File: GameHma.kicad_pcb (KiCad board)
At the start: 2 copper layers, 98 x 82 mm, 19 parts, among them J1 Screw_Terminal_01x02, J2 Motor_Terminal_01x04, J3 Motor_Terminal_01x04, J4 Motor_Terminal_01x04, J5 Motor_Terminal_01x04, U1 ESP32-DEVKIT-V1, U2 A4988_STEPPER_MOTOR_DRIVER_CA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, U3 A4988_STEPPER_MOTOR_DRIVER_CA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, U4 A4988_STEPPER_MOTOR_DRIVER_CA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, U5 A4988_STEPPER_MOTOR_DRIVER_CA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, U6 SRT_MP1584EN

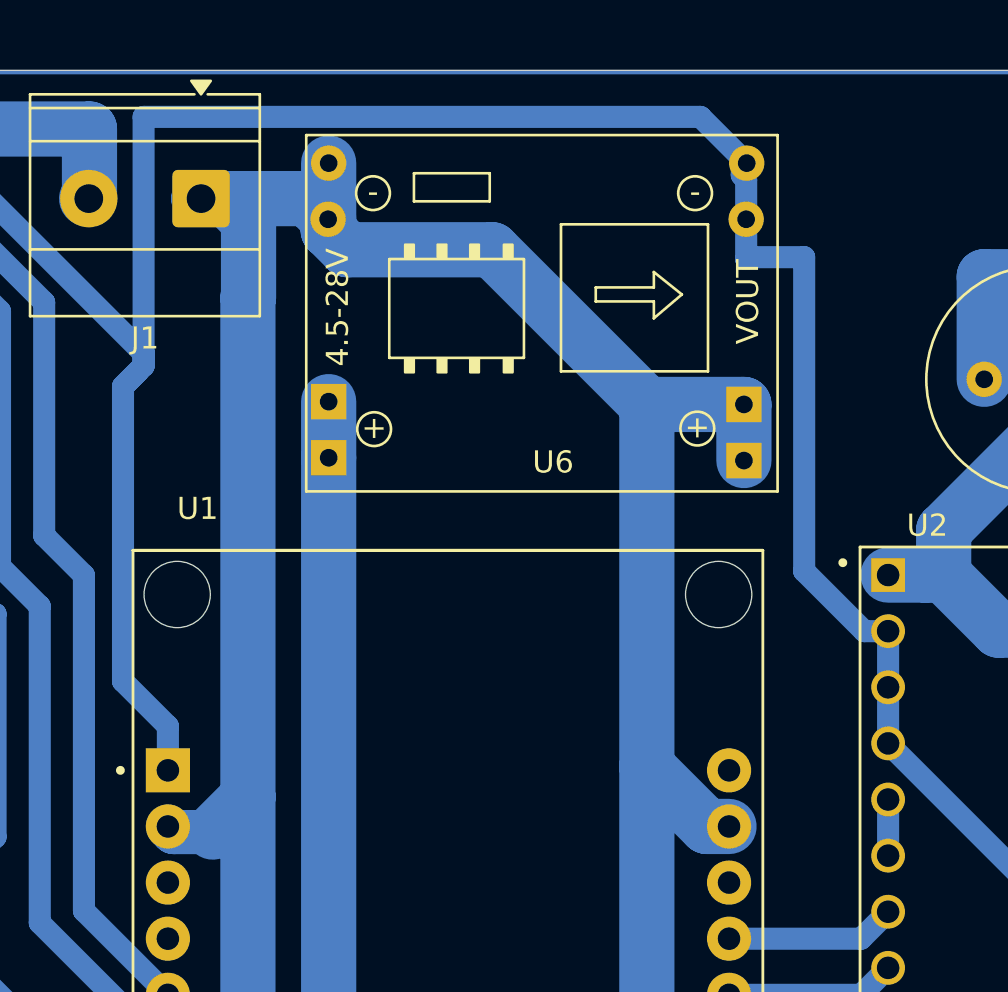
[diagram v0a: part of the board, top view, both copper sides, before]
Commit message: fix pin MP1584 footprint
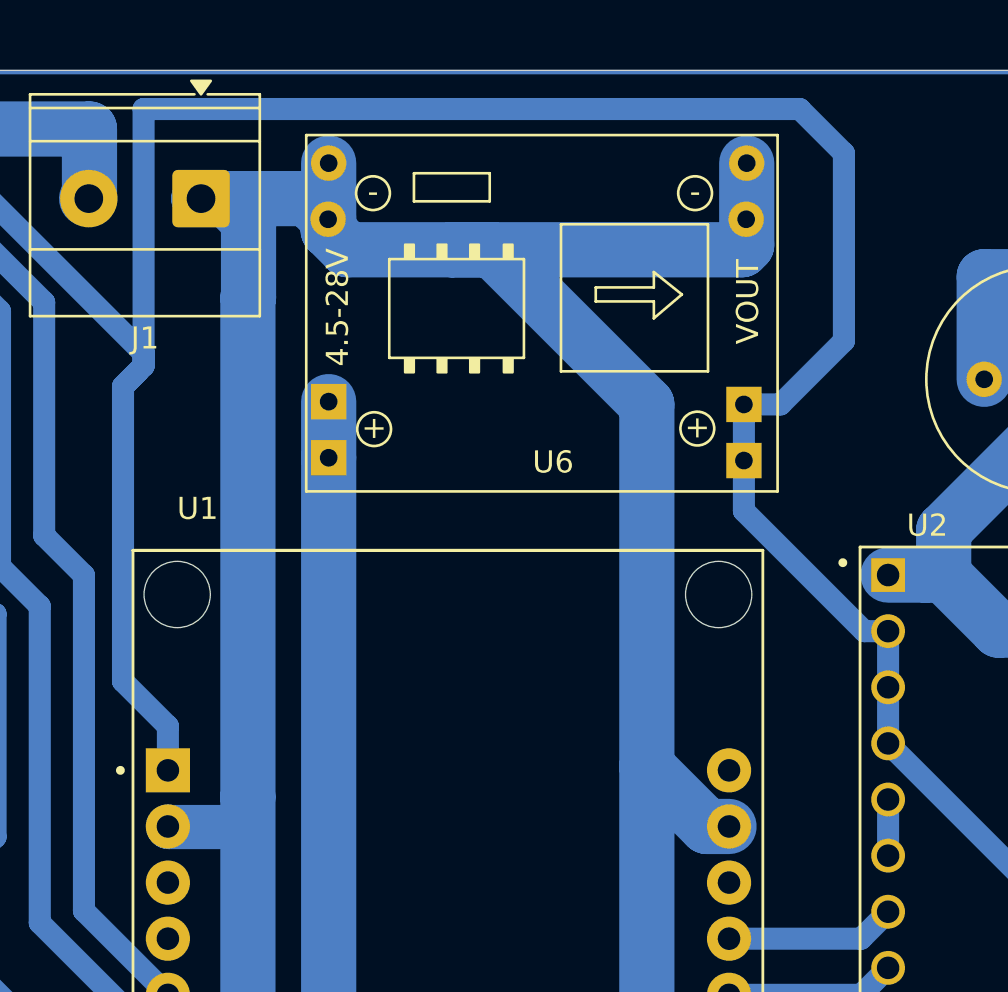
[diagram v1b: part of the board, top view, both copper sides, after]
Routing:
- net GND: track 467.1 -> 477.7 mm
- net +V_{DD}: track 252.3 -> 258.4 mm

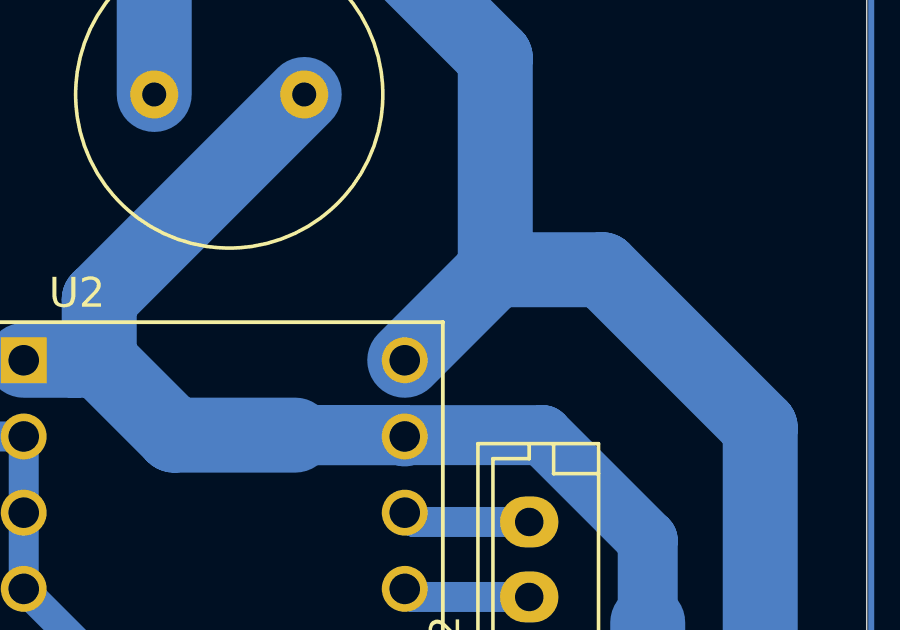
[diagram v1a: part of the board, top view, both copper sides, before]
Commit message: edit wire in U2 pin Vbatt at PCB editor
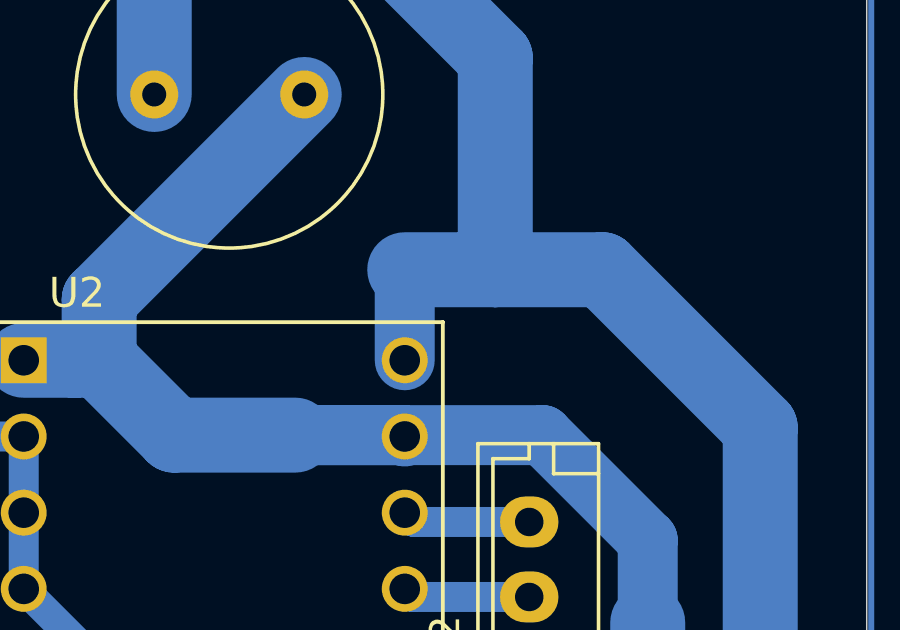
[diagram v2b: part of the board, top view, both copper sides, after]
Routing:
- net +V_{batt}: track 391.5 -> 393.2 mm
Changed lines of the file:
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@@
-	)
-	(segment
-		(start 182.2179 78.8271)
-		(end 179.2 81.845)
-		(width 2.5)
-		(layer "B.Cu")
-		(net 2)
 	)
 	(segment
@@
 	)
 	(segment
+		(start 182.2179 78.8271)
+		(end 179.2 78.8271)
+		(width 2.5)
+		(layer "B.Cu")
+		(net 2)
+	)
+	(segment
 		(start 110.95 122.655)
 		(end 100.5 122.655)
@@
 		(layer "B.Cu")
 		(net 2)
+	)
+	(segment
+		(start 179.2 81.845)
+		(end 179.2 78.8271)
+		(width 2)
+		(layer "B.Cu")
+		(net 2)

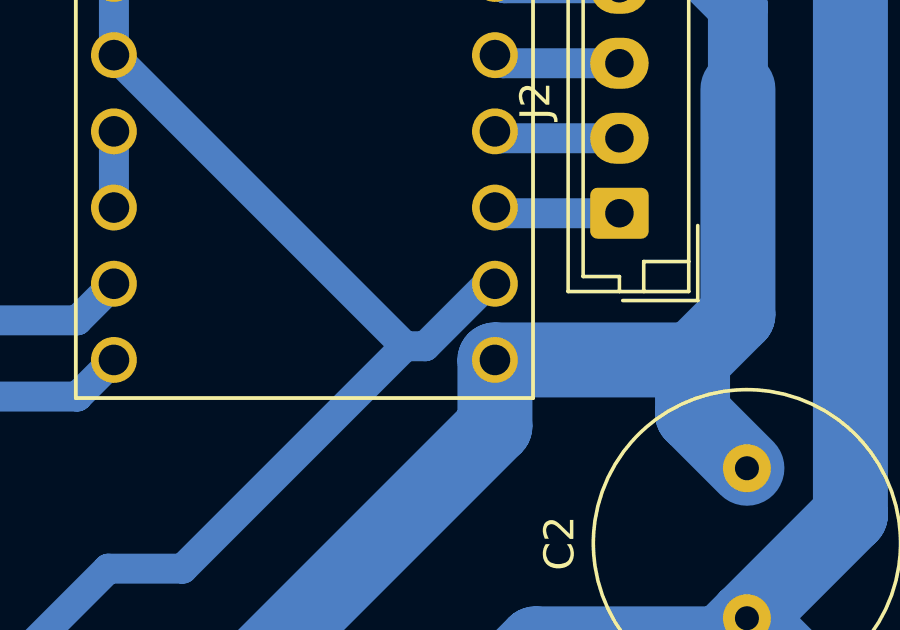
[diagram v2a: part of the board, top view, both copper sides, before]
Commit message: edit wire in U2 pin VDD at PCB editor
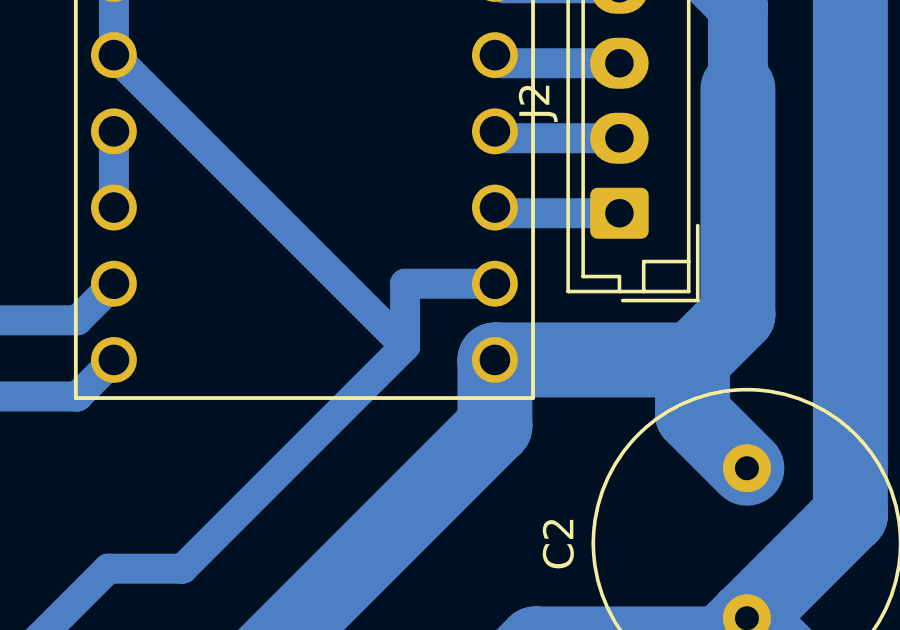
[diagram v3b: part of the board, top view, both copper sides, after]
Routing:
- net +V_{DD}: track 258.4 -> 259.6 mm
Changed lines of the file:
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@@
-	)
-	(segment
-		(start 179.2 97.085)
-		(end 178.9623 97.085)
-		(width 1)
-		(layer "B.Cu")
-		(net 27)
 	)
 	(segment
@@
 	)
 	(segment
+		(start 176.2046 99.1687)
+		(end 176.2042 99.1691)
+		(width 1)
+		(layer "B.Cu")
+		(net 27)
+	)
+	(segment
 		(start 132.8 72.3733)
 		(end 131.8683 73.305)
@@
 	)
 	(segment
+		(start 176.2046 97.085)
+		(end 176.2046 99.1687)
+		(width 1)
+		(layer "B.Cu")
+		(net 27)
+	)
+	(segment
 		(start 162.5 60.75)
 		(end 164.5 62.75)
@@
 	)
 	(segment
-		(start 176.2046 99.1687)
-		(end 176.2042 99.1691)
+		(start 179.2 97.085)
+		(end 176.2046 97.085)
 		(width 1)
 		(layer "B.Cu")
@@
 	)
 	(segment
-		(start 176.8786 99.1687)
-		(end 176.2046 99.1687)
-		(width 1)
-		(layer "B.Cu")
-		(net 27)
-	)
-	(segment
 		(start 161.628 74.122)
 		(end 159.973 74.122)
 		(width 1)
 		(layer "B.Cu")
-		(net 27)
-	)
-	(segment
-		(start 178.9623 97.085)
-		(end 176.8786 99.1687)
-		(width 1)
-		(layer "B.Cu")
